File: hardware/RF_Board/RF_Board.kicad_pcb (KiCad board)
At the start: 4 copper layers, 90 x 90 mm, 130 parts, among them J1 Conn_Coaxial, J2 Conn_01x04_Male, J3 Conn_Coaxial, J4 Conn_01x04_Male, J5 Conn_01x06_Female, J6 Conn_01x06_Female, J7 Conn_01x06_Female, J8 L77TSAH15SOL2RM8, Q1 2N7002, Q2 2N7002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

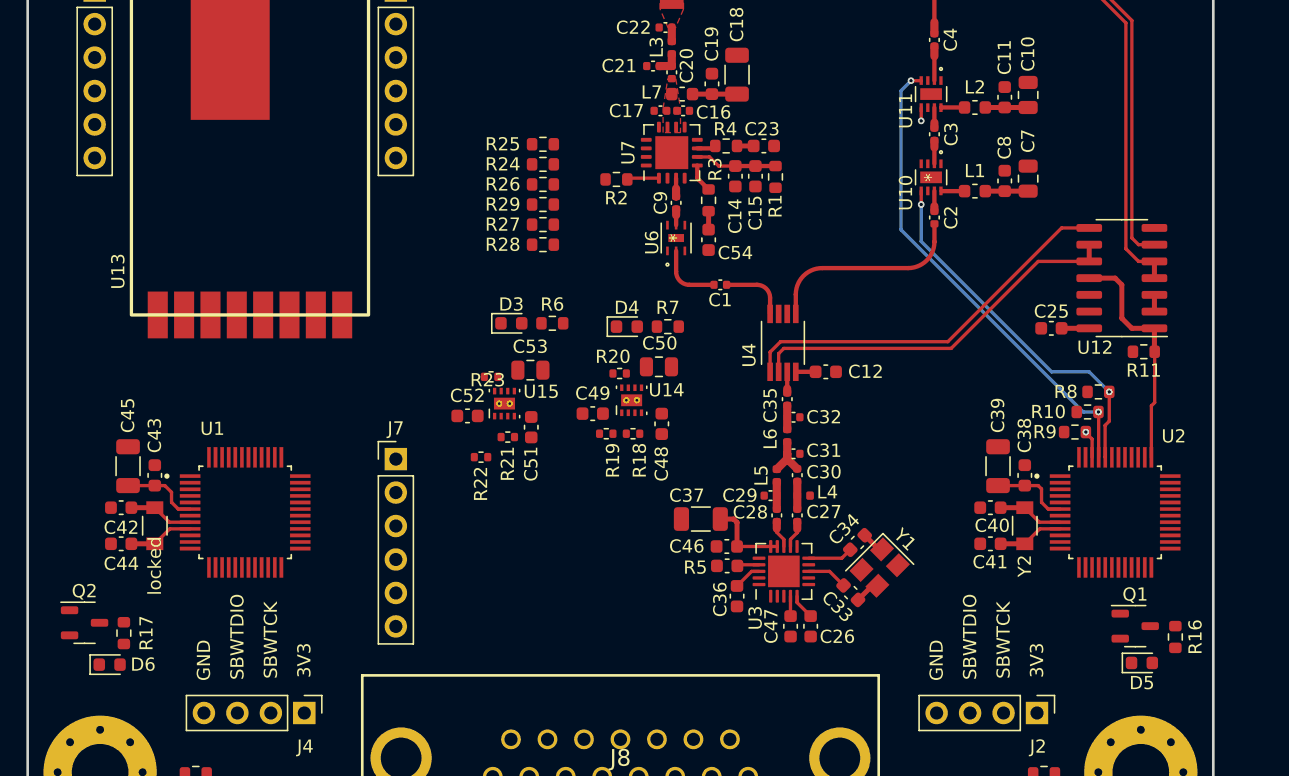
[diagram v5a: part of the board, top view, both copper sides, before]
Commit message: add SMA connector 3D model
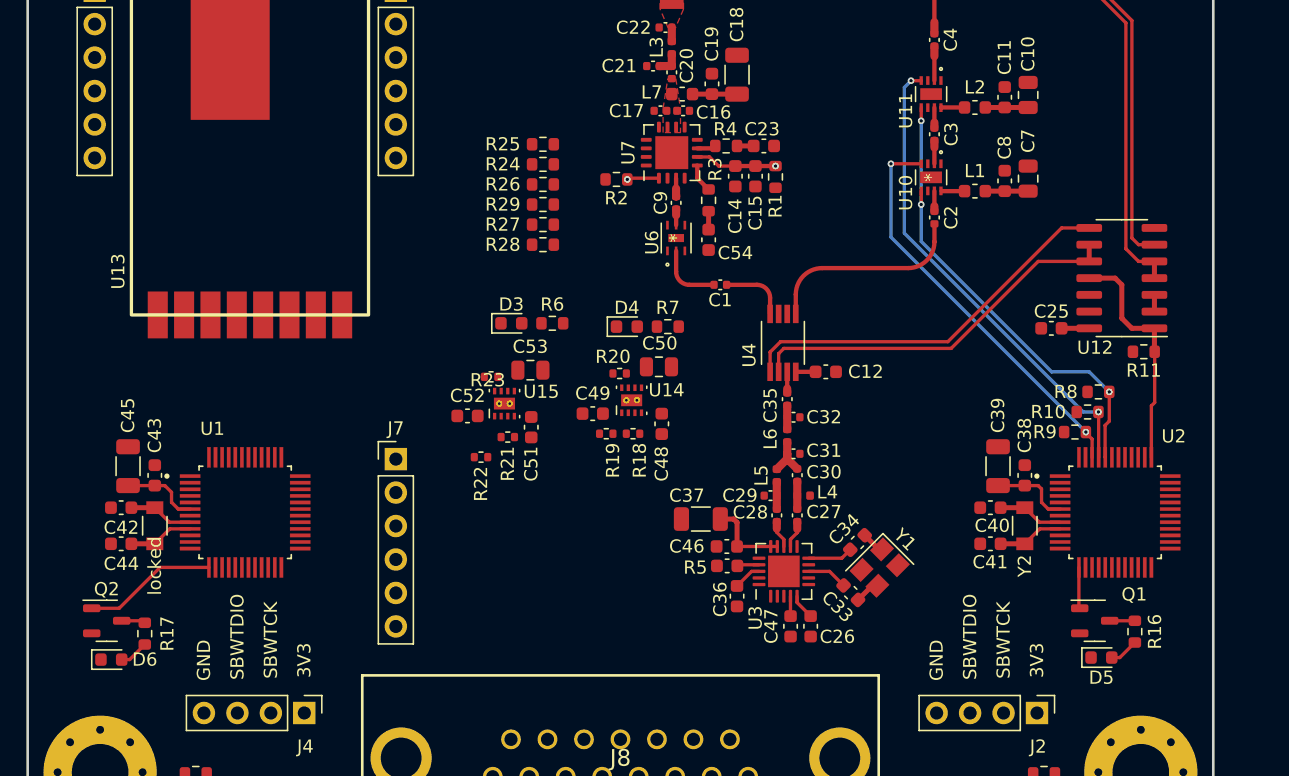
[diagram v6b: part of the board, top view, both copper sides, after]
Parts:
- moved D5 3.10 mm to (81.5, 75.8)
- moved Q1 3.10 mm to (81.0, 73.0)
- moved R16 3.10 mm to (84.0, 73.8)
- moved Q2 1.69 mm to (6.00, 73.0)
- moved R17 1.59 mm to (8.89, 74.0)
- moved D6 0.40 mm to (6.35, 75.9)
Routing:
- net /LNA_BP_A: track 2.11 -> 30.9 mm, vias 1 -> 2
- net /RFM_MOSI: track 0.00 -> 10.2 mm
- net /LNA_SD: track 28.9 -> 35.3 mm
- net /CC2500_MOSI: track 0.00 -> 3.13 mm
- net Net-(D6-Pad2): track 0.00 -> 2.23 mm
- net Net-(D5-Pad2): track 0.00 -> 2.23 mm
- net Net-(Q1-Pad3): track 0.00 -> 1.91 mm
- net Net-(Q2-Pad3): track 0.00 -> 1.82 mm
- net /PA_VDET: vias 0 -> 1
- net /PA_EN: vias 0 -> 1
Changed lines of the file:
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@@
   )
   (footprint "RF_Board_Footprints:LED_0603_1608Metric" (layer "F.Cu")
-    (at 6.223 76.327)
+    (at 6.35 75.946)
     (descr "LED SMD 0603 (1608 Metric), square (rectangular) end terminal, IPC_7351 nominal, (Body size source: http://www.tortai-tech.com/upload/download/2011102023233369053.pdf), generated with kicad-footprint-generator")
     (tags "LED")
@@
   )
   (footprint "RF_Board_Footprints:LED_0603_1608Metric" (layer "F.Cu")
-    (at 84.582 76.2)
+    (at 81.508 75.794)
     (descr "LED SMD 0603 (1608 Metric), square (rectangular) end terminal, IPC_7351 nominal, (Body size source: http://www.tortai-tech.com/upload/download/2011102023233369053.pdf), generated with kicad-footprint-generator")
     (tags "LED")
@@
   )
   (footprint "RF_Board_Footprints:R_0603_1608Metric" (layer "F.Cu")
-    (at 87.122 74.231 90)
+    (at 84.048 73.825 90)
     (descr "Resistor SMD 0603 (1608 Metric), square (rectangular) end terminal, IPC_7351 nominal, (Body size source: IPC-SM-782 page 72, https://www.pcb-3d.com/wordpress/wp-content/uploads/ipc-sm-782a_amendment_1_and_2.pdf), generated with kicad-footprint-generator")
     (tags "resistor")
@@
     (pad "2" thru_hole circle locked (at -2.54 2.54 180) (size 2.25 2.25) (drill 1.7) (layers *.Cu *.Mask)
       (net 13 "GND") (pinfunction "Ext") (pintype "passive"))
-    (model "${KICAD6_3DMODEL_DIR}/Connector_Coaxial.3dshapes/SMA_Amphenol_901-144_Vertical.wrl"
+    (model "${KICAD6_3DMODEL_DIR}/Connector_Coaxial.3dshapes/SMA_Amphenol_901-144_Vertical.wrl" hide
       (offset (xyz 0 0 0))
       (scale (xyz 1 1 1))
       (rotate (xyz 0 0 0))
     )
+    (model "${KIPRJMOD}/3D_Models/73251-3140.stp"
+      (offset (xyz 0 0 6.5))
+      (scale (xyz 1 1 1))
+      (rotate (xyz 0 -90 0))
+    )
   )
   (footprint "RF_Board_Footprints:C_0402_1005Metric" (layer "F.Cu")
@@
   )
   (footprint "RF_Board_Footprints:SOT-23-3" (layer "F.Cu")
-    (at 84.074 73.406)
+    (at 81 73)
     (descr "SOT, 3 Pin (https://www.jedec.org/sites/default/files/docs/Mo-178D.PDF inferred 3-pin variant), generated with kicad-footprint-generator ipc_gullwing_generator.py")
     (tags "SOT TO_SOT_SMD")
@@
     (property "Sheetname" "")
     (attr smd)
-    (fp_text reference "Q1" (at 0 -2.4) (layer "F.SilkS")
+    (fp_text reference "Q1" (at 3 -2) (layer "F.SilkS")
       (effects (font (size 1 1) (thickness 0.15)))
     )
@@
   )
   (footprint "RF_Board_Footprints:SOT-23-3" (layer "F.Cu")
-    (at 4.318 73.152)
+    (at 6 73)
     (descr "SOT, 3 Pin (https://www.jedec.org/sites/default/files/docs/Mo-178D.PDF inferred 3-pin variant), generated with kicad-footprint-generator ipc_gullwing_generator.py")
     (tags "SOT TO_SOT_SMD")
@@
       (rotate (xyz 0 0 0))
     )
+    (model "${KIPRJMOD}/3D_Models/73251-3140.stp"
+      (offset (xyz 0 0 6.5))
+      (scale (xyz 1 1 1))
+      (rotate (xyz 0 -90 0))
+    )
   )
   (footprint "RF_Board_Footprints:SOIC-14_3.9x8.7mm_P1.27mm" (layer "F.Cu")
@@
   )
   (footprint "RF_Board_Footprints:R_0603_1608Metric" (layer "F.Cu")
-    (at 7.303 73.937 90)
+    (at 8.89 73.977 90)
     (descr "Resistor SMD 0603 (1608 Metric), square (rectangular) end terminal, IPC_7351 nominal, (Body size source: IPC-SM-782 page 72, https://www.pcb-3d.com/wordpress/wp-content/uploads/ipc-sm-782a_amendment_1_and_2.pdf), generated with kicad-footprint-generator")
     (tags "resistor")
@@
     )
   )
+  (gr_line (start 83 16) (end 83 17) (layer "B.SilkS") (width 0.15))
+  (gr_line (start 73 16) (end 73 17) (layer "B.SilkS") (width 0.15))
+  (gr_line (start 88 26) (end 86 26) (layer "B.SilkS") (width 0.15))
+  (gr_line (start 88 16) (end 88 36) (layer "B.SilkS") (width 0.15))
+  (gr_line (start 88 16) (end 68 16) (layer "B.SilkS") (width 0.15))
+  (gr_line (start 78 16) (end 78 18) (layer "B.SilkS") (width 0.15))
+  (gr_line (start 88 21) (end 87 21) (layer "B.SilkS") (width 0.15))
+  (gr_line (start 88 31) (end 87 31) (layer "B.SilkS") (width 0.15))
   (gr_arc (start 87.46 0) (mid 89.256051 0.743949) (end 90 2.54) (layer "Edge.Cuts") (width 0.2))
   (gr_line (start 87.46 90) (end 2.54 90) (layer "Edge.Cuts") (width 0.2))
@@
   (segment (start 51.76 37.79) (end 52.451 38.481) (width 0.254) (layer "F.Cu") (net 17))
   (segment (start 56.769 38.481) (end 53.721 38.481) (width 0.3302) (layer "F.Cu") (net 17))
+  (via (at 56.769 38.481) (size 0.508) (drill 0.254) (layers "F.Cu" "B.Cu") (net 17))
   (segment (start 47.953004 30.891282) (end 48.892718 30.891282) (width 0.62) (layer "F.Cu") (net 18))
   (segment (start 48.892718 30.891282) (end 48.895 30.889) (width 0.62) (layer "F.Cu") (net 18))
@@
   (segment locked (start 12.33 66.02) (end 10.7896 66.02) (width 0.254) (layer "F.Cu") (net 38))
   (segment locked (start 7.874 67.1576) (end 9.652 67.1576) (width 0.381) (layer "F.Cu") (net 38))
+  (segment (start 82.904 75.794) (end 84.048 74.65) (width 0.254) (layer "F.Cu") (net 45))
+  (segment (start 82.2955 75.794) (end 82.904 75.794) (width 0.254) (layer "F.Cu") (net 45))
+  (segment (start 8.89 74.802) (end 7.746 75.946) (width 0.254) (layer "F.Cu") (net 46))
+  (segment (start 7.746 75.946) (end 7.1375 75.946) (width 0.254) (layer "F.Cu") (net 46))
+  (segment (start 4.8625 72.05) (end 6.95 72.05) (width 0.254) (layer "F.Cu") (net 63))
+  (segment (start 6.95 72.05) (end 10.05 68.95) (width 0.254) (layer "F.Cu") (net 63))
+  (segment (start 10.05 68.95) (end 13.76 68.95) (width 0.254) (layer "F.Cu") (net 63))
   (segment (start 71.12 40.386) (end 69.360263 40.386) (width 0.3302) (layer "F.Cu") (net 86))
   (segment (start 71.103363 34.0487) (end 71.116063 34.036) (width 0.3302) (layer "F.Cu") (net 87))
   (segment (start 71.116063 34.036) (end 69.360263 34.036) (width 0.3302) (layer "F.Cu") (net 87))
   (segment (start 69.360263 34.036) (end 69.360263 34.0487) (width 0.3302) (layer "F.Cu") (net 87))
+  (segment (start 79.8 68.95) (end 79.8 71.9875) (width 0.254) (layer "F.Cu") (net 88))
+  (segment (start 79.8 71.9875) (end 79.8625 72.05) (width 0.254) (layer "F.Cu") (net 88))
+  (segment (start 82.1375 73) (end 84.048 73) (width 0.254) (layer "F.Cu") (net 89))
+  (segment (start 7.1375 73) (end 8.738 73) (width 0.254) (layer "F.Cu") (net 90))
+  (segment (start 8.738 73) (end 8.89 73.152) (width 0.254) (layer "F.Cu") (net 90))
   (segment (start 45.6125 39.4025) (end 45.518 39.497) (width 0.254) (layer "F.Cu") (net 91))
   (segment (start 47.92 39.4025) (end 45.6125 39.4025) (width 0.254) (layer "F.Cu") (net 91))
+  (via (at 45.518 39.497) (size 0.508) (drill 0.254) (layers "F.Cu" "B.Cu") (net 91))
   (segment (start 50.8325 39.4025) (end 51.689 40.259) (width 0.3302) (layer "F.Cu") (net 92))
   (segment (start 50.8325 38.44) (end 50.8325 39.4025) (width 0.3302) (layer "F.Cu") (net 92))
@@
   (segment (start 77.724 54.102) (end 67.8298 44.2078) (width 0.254) (layer "B.Cu") (net 95))
   (segment (start 82.105 55.626) (end 80.581 54.102) (width 0.254) (layer "B.Cu") (net 95))
+  (segment (start 67.8298 41.402) (end 67.8298 35.052) (width 0.254) (layer "B.Cu") (net 95))
   (segment (start 80.327 58.674) (end 80.327 58.737) (width 0.254) (layer "F.Cu") (net 96))
   (segment (start 80.8 59.21) (end 80.8 60.59) (width 0.254) (layer "F.Cu") (net 96))
   (segment (start 80.327 58.737) (end 80.8 59.21) (width 0.254) (layer "F.Cu") (net 96))
+  (segment (start 65.532 38.3103) (end 67.829811 38.3103) (width 0.254) (layer "F.Cu") (net 96))
   (via (at 80.327 58.674) (size 0.508) (drill 0.254) (layers "F.Cu" "B.Cu") (net 96))
+  (via (at 65.532 38.3103) (size 0.508) (drill 0.254) (layers "F.Cu" "B.Cu") (free) (net 96))
+  (segment (start 80.327 58.674) (end 65.532 43.879) (width 0.254) (layer "B.Cu") (net 96))
+  (segment (start 65.532 43.879) (end 65.532 38.3103) (width 0.254) (layer "B.Cu") (net 96))
   (segment (start 81.3 57.166) (end 81.284 57.15) (width 0.254) (layer "F.Cu") (net 97))
   (segment (start 67.817111 32.004) (end 67.829811 31.9913) (width 0.254) (layer "F.Cu") (net 97))
@@
   (via (at 81.284 57.15) (size 0.508) (drill 0.254) (layers "F.Cu" "B.Cu") (net 97))
   (via (at 67.056 32.004) (size 0.508) (drill 0.254) (layers "F.Cu" "B.Cu") (free) (net 97))
-  (segment (start 80.129948 57.15) (end 66.294 43.314052) (width 0.254) (layer "B.Cu") (net 97))
-  (segment (start 66.294 43.314052) (end 66.294 32.766) (width 0.254) (layer "B.Cu") (net 97))
-  (segment (start 66.294 32.766) (end 67.056 32.004) (width 0.254) (layer "B.Cu") (net 97))
+  (segment (start 66.548 32.512) (end 67.056 32.004) (width 0.254) (layer "B.Cu") (net 97))
+  (segment (start 66.548 43.568052) (end 66.548 32.512) (width 0.254) (layer "B.Cu") (net 97))
+  (segment (start 80.129948 57.15) (end 66.548 43.568052) (width 0.254) (layer "B.Cu") (net 97))
   (segment (start 81.284 57.15) (end 80.129948 57.15) (width 0.254) (layer "B.Cu") (net 97))
   (segment (start 83.058 47.498) (end 82.55 46.99) (width 0.381) (layer "F.Cu") (net 98))

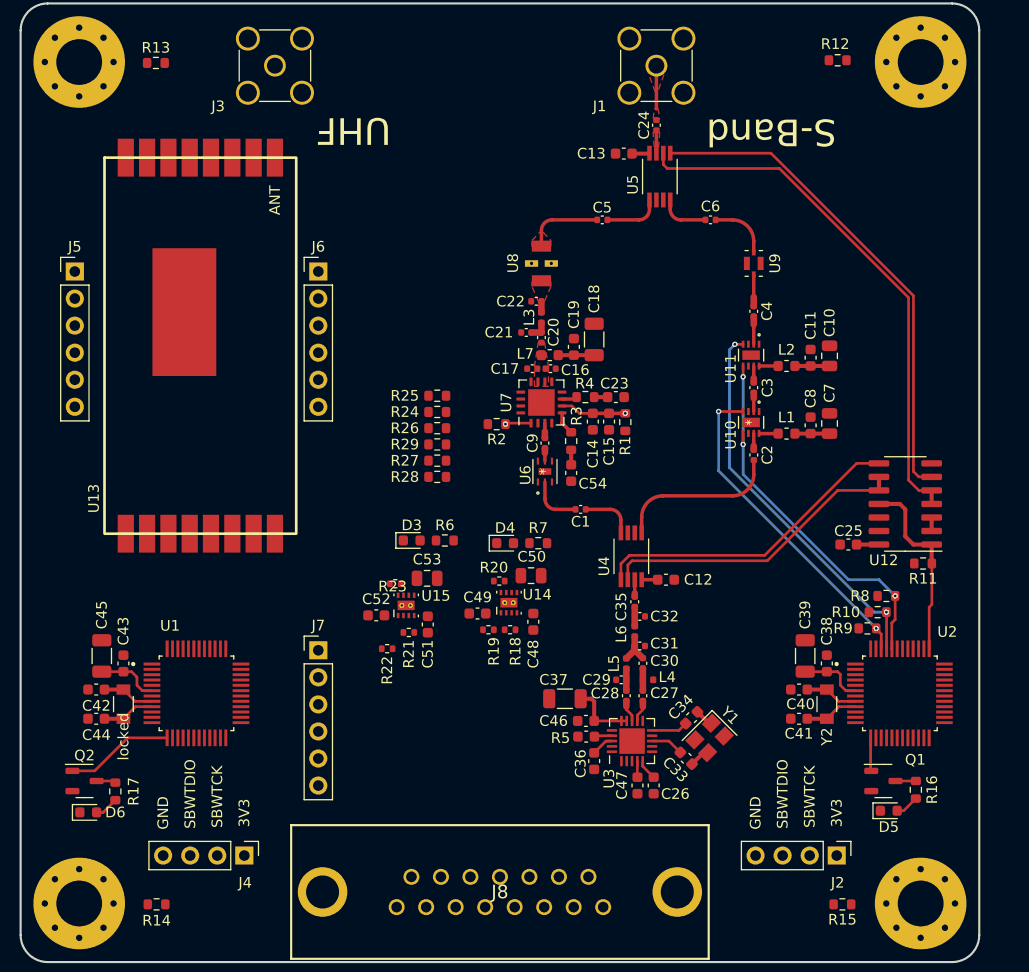
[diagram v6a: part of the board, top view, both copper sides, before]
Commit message: RF board digital routing
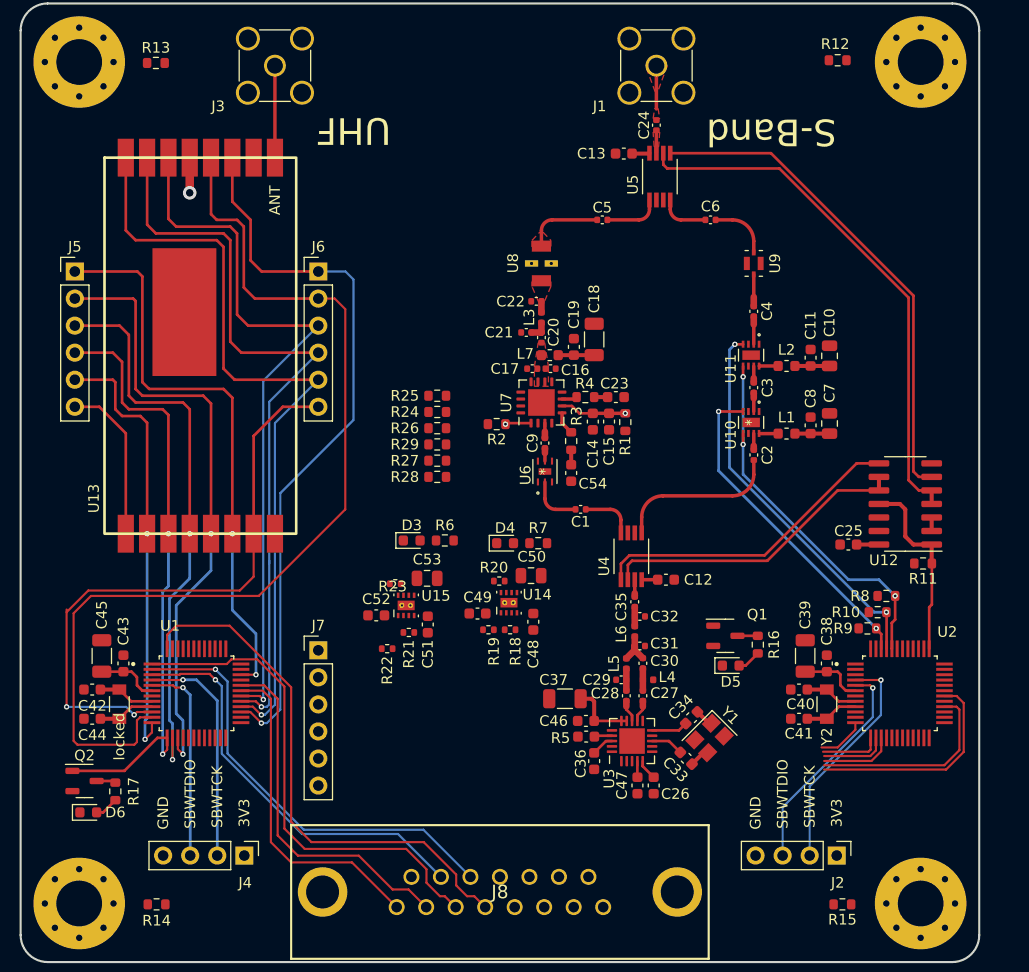
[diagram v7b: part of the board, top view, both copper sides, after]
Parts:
- moved Q1 20.1 mm to (66.2, 59.4)
- moved R16 20.1 mm to (69.2, 60.2)
- moved D5 20.1 mm to (66.7, 62.2)
- moved C42 0.38 mm to (6.72, 64.4)
- moved C44 0.38 mm to (6.72, 67.2)
- moved locked 0.38 mm to (9.27, 65.8)
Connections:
- U1 pad 1: /RFM_RX_EMPTY -> /RFM_TX_EMPTY
- U1 pad 2: /RFM_TX_OVERFLOW -> /RFM_RX_OVERFLOW
- U1 pad 3: /RFM_RX_OVERFLOW -> /RFM_TX_OVERFLOW
- U1 pad 48: /RFM_TX_EMPTY -> /RFM_RX_EMPTY
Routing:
- net /RFM_DIO4: track 0.00 -> 95.0 mm
- net /RFM_DIO2: track 0.00 -> 73.5 mm, vias 0 -> 1
- net /RFM_DIO1: track 0.00 -> 71.0 mm, vias 0 -> 1
- net /RFM_DIO3: track 0.00 -> 68.6 mm, vias 0 -> 1
- net /RFM_DIO0: track 0.00 -> 67.9 mm, vias 0 -> 1
- net /RFM_CSN: track 0.00 -> 58.0 mm, vias 0 -> 2
- net /RFM_DIO5: track 0.00 -> 56.9 mm, vias 0 -> 2
- net /RFM_RST: track 0.00 -> 53.8 mm, vias 0 -> 2
- net /RFM_SCLK: track 0.00 -> 53.2 mm, vias 0 -> 2
- net /RFM_RX_EMPTY: track 0.00 -> 50.5 mm
- net /RFM_MOSI: track 10.2 -> 57.4 mm, vias 0 -> 2
- net /RFM_TX_EMPTY: track 0.00 -> 46.9 mm
- net /RFM_RX_OVERFLOW: track 0.00 -> 41.9 mm, vias 0 -> 1
- net /RFM_MISO: track 0.00 -> 41.6 mm, vias 0 -> 2
- net /RFM_TX_OVERFLOW: track 0.00 -> 38.8 mm, vias 0 -> 1
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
